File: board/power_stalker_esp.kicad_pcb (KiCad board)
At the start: 2 copper layers, 43.5 x 61 mm, 10 parts, among them J1 POWER IN, J2 LEFT, J3 RIGHT, Q1 Phototrans, Q2 Q_NPN_BEC, U1 74HC393

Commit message: Generated gerber files.
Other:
- board text added: "REV A 11/2018"
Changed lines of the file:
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@@
   (general
     (thickness 1.6)
-    (drawings 746)
+    (drawings 747)
     (tracks 104)
     (zones 0)
@@
     (visible_elements 7FFFFFFF)
     (pcbplotparams
-      (layerselection 0x010fc_ffffffff)
+      (layerselection 0x010f0_ffffffff)
       (usegerberextensions false)
       (usegerberattributes false)
@@
       (outputformat 1)
       (mirror false)
-      (drillshape 1)
+      (drillshape 0)
       (scaleselection 1)
-      (outputdirectory ""))
+      (outputdirectory "Gerbers"))
   )
   (net 0 "")
@@
     )
   )
+  (gr_text "REV A\n11/2018" (at 97.6 115.8) (layer B.SilkS)
+    (effects (font (size 1.5 1.5) (thickness 0.3)) (justify mirror))
+  )
   (gr_line (start 94.725 126.9) (end 94.025 126.9) (layer F.SilkS) (width 0.2))

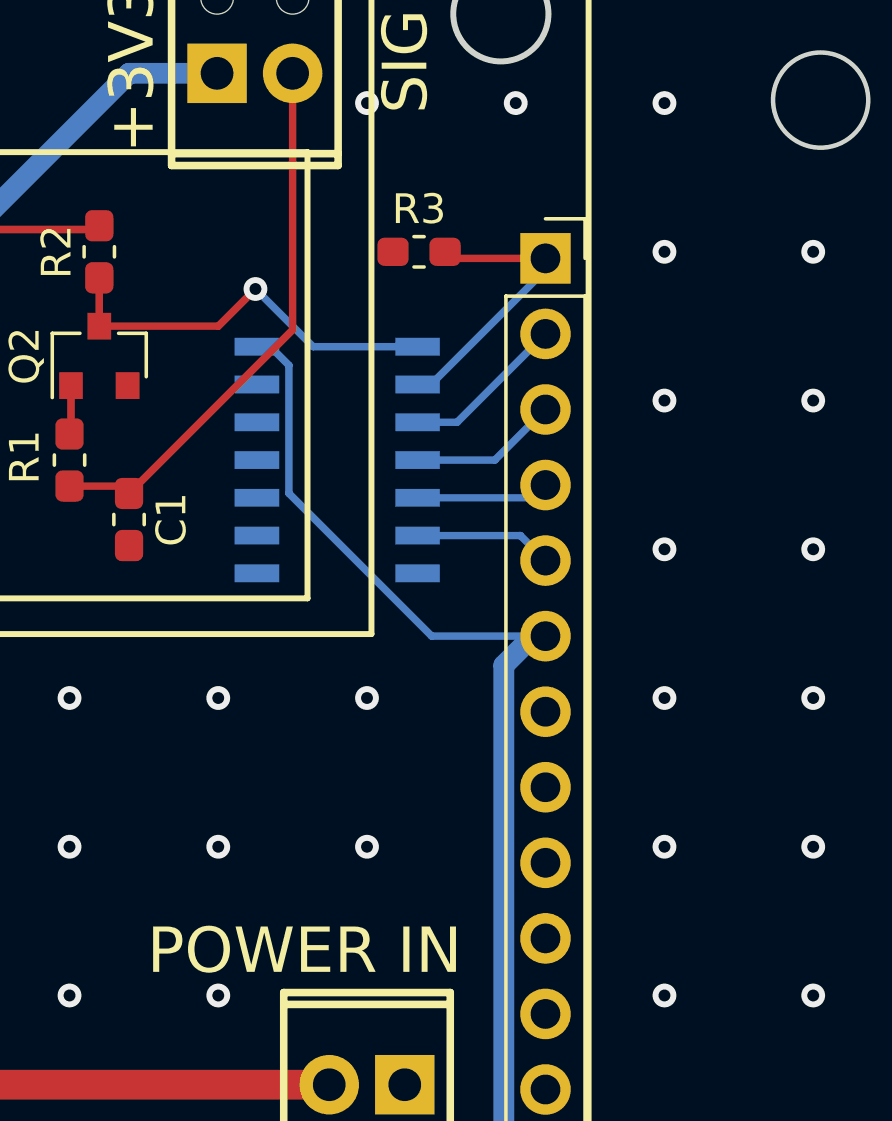
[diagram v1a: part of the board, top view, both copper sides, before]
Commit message: /!\ Moved some GPIO (D0,D3 and D4 seem to not be real GPIOs...)
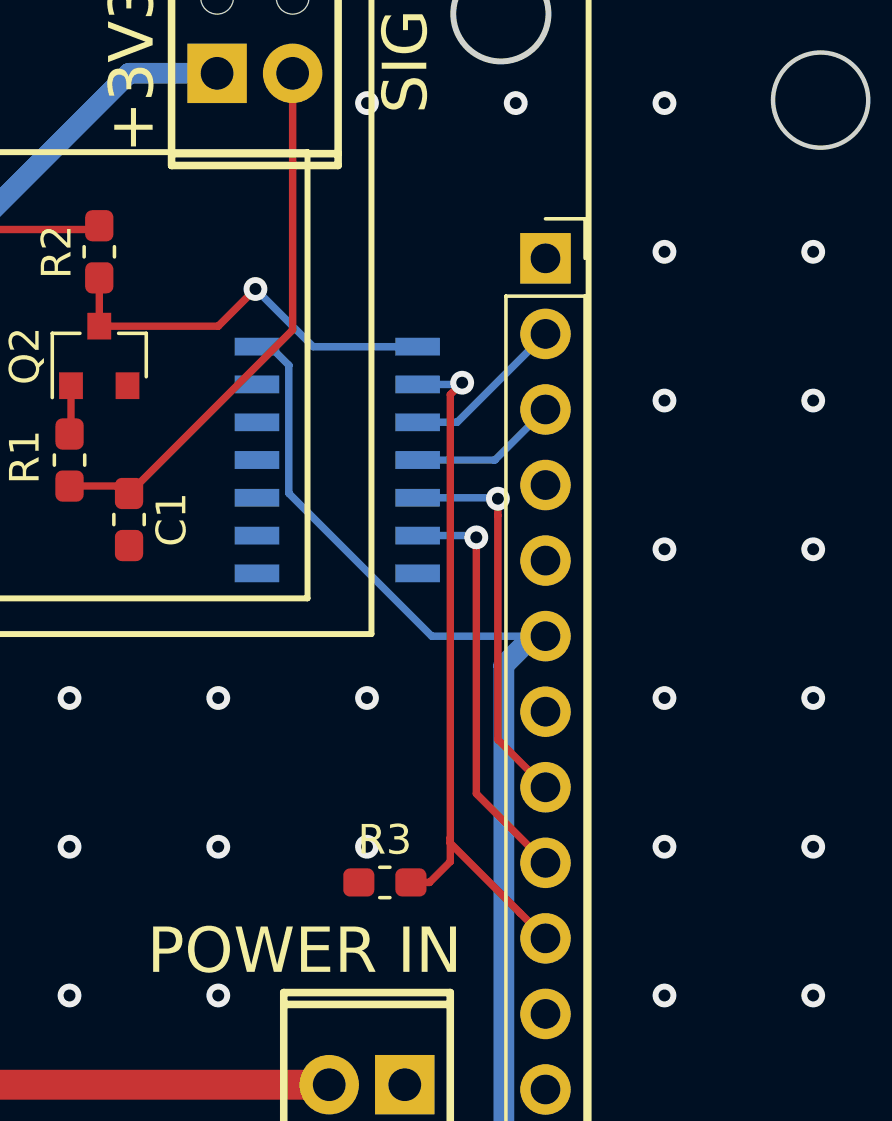
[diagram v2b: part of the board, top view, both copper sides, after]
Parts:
- C1: value 0.1uF/25V -> 0.1uF/50V
- moved R3 21.2 mm to (100.6, 101.2)
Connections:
- J3 pad 1: MASTER_RESET -> (no net)
- J3 pad 10: (no net) -> MASTER_RESET
- J3 pad 4: 1Q2 -> (no net)
- J3 pad 5: 1Q3 -> (no net)
- J3 pad 8: (no net) -> 1Q2
- J3 pad 9: (no net) -> 1Q3
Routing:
- net MASTER_RESET: track 9.75 -> 24.1 mm, vias 0 -> 1
- net 1Q3: track 4.65 -> 13.9 mm, vias 0 -> 1
- net 1Q2: track 4.48 -> 13.1 mm, vias 0 -> 1
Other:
- board text added: "REV B 06/2019"
- board text removed: "REV A 11/2018"
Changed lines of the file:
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@@
-(kicad_pcb (version 20171130) (host pcbnew "(5.0.1)-3")
+(kicad_pcb (version 20171130) (host pcbnew "(5.1.2)-2")
   (general
     (thickness 1.6)
     (drawings 747)
-    (tracks 104)
+    (tracks 117)
     (zones 0)
     (modules 10)
@@
     (zone_45_only no)
     (trace_min 0.2)
-    (segment_width 0.2)
-    (edge_width 0.2)
     (via_size 0.8)
     (via_drill 0.4)
@@
     (uvia_min_size 0.2)
     (uvia_min_drill 0.1)
+    (edge_width 0.2)
+    (segment_width 0.2)
     (pcb_text_width 0.3)
     (pcb_text_size 1.5 1.5)
@@
     (solder_mask_min_width 0.25)
     (aux_axis_origin 0 0)
-    (grid_origin 79.5 124)
     (visible_elements 7FFFFFFF)
     (pcbplotparams
@@
       (effects (font (size 1 1) (thickness 0.15)))
     )
-    (fp_text value 0.1uF/25V (at 0 1.43 270) (layer F.Fab)
+    (fp_text value 0.1uF/50V (at 0 1.43 270) (layer F.Fab)
       (effects (font (size 1 1) (thickness 0.15)))
     )
@@
     (pad 12 thru_hole oval (at 0 27.94) (size 1.7 1.7) (drill 1) (layers *.Cu *.Mask))
     (pad 11 thru_hole oval (at 0 25.4) (size 1.7 1.7) (drill 1) (layers *.Cu *.Mask))
-    (pad 10 thru_hole oval (at 0 22.86) (size 1.7 1.7) (drill 1) (layers *.Cu *.Mask))
-    (pad 9 thru_hole oval (at 0 20.32) (size 1.7 1.7) (drill 1) (layers *.Cu *.Mask))
-    (pad 8 thru_hole oval (at 0 17.78) (size 1.7 1.7) (drill 1) (layers *.Cu *.Mask))
+    (pad 10 thru_hole oval (at 0 22.86) (size 1.7 1.7) (drill 1) (layers *.Cu *.Mask)
+      (net 9 MASTER_RESET))
+    (pad 9 thru_hole oval (at 0 20.32) (size 1.7 1.7) (drill 1) (layers *.Cu *.Mask)
+      (net 5 1Q3))
+    (pad 8 thru_hole oval (at 0 17.78) (size 1.7 1.7) (drill 1) (layers *.Cu *.Mask)
+      (net 6 1Q2))
     (pad 7 thru_hole oval (at 0 15.24) (size 1.7 1.7) (drill 1) (layers *.Cu *.Mask)
       (net 2 GND))
     (pad 6 thru_hole oval (at 0 12.7) (size 1.7 1.7) (drill 1) (layers *.Cu *.Mask)
       (net 4 +3V3))
-    (pad 5 thru_hole oval (at 0 10.16) (size 1.7 1.7) (drill 1) (layers *.Cu *.Mask)
-      (net 5 1Q3))
-    (pad 4 thru_hole oval (at 0 7.62) (size 1.7 1.7) (drill 1) (layers *.Cu *.Mask)
-      (net 6 1Q2))
+    (pad 5 thru_hole oval (at 0 10.16) (size 1.7 1.7) (drill 1) (layers *.Cu *.Mask))
+    (pad 4 thru_hole oval (at 0 7.62) (size 1.7 1.7) (drill 1) (layers *.Cu *.Mask))
     (pad 3 thru_hole oval (at 0 5.08) (size 1.7 1.7) (drill 1) (layers *.Cu *.Mask)
       (net 7 1Q1))
     (pad 2 thru_hole oval (at 0 2.54) (size 1.7 1.7) (drill 1) (layers *.Cu *.Mask)
       (net 8 1Q0))
-    (pad 1 thru_hole rect (at 0 0) (size 1.7 1.7) (drill 1) (layers *.Cu *.Mask)
-      (net 9 MASTER_RESET))
+    (pad 1 thru_hole rect (at 0 0) (size 1.7 1.7) (drill 1) (layers *.Cu *.Mask))
     (model ${KISYS3DMOD}/Connector_PinSocket_2.54mm.3dshapes/PinSocket_1x15_P2.54mm_Vertical.wrl
       (at (xyz 0 0 0))
@@
   )
   (module Resistor_SMD:R_0603_1608Metric_Pad1.05x0.95mm_HandSolder (layer F.Cu)
-    (at 101.75 80)
+    (at 100.6 101.2)
     (descr "Resistor SMD 0603 (1608 Metric), square (rectangular) end terminal, IPC_7351 nominal with elongated pad for handsoldering. (Body size source: http://www.tortai-tech.com/upload/download/2011102023233369053.pdf), generated with kicad-footprint-generator")
     (tags "resistor handsolder")
@@
     )
   )
-  (gr_text "REV A\n11/2018" (at 97.6 115.8) (layer B.SilkS)
+  (gr_text "REV B\n06/2019" (at 97.6 115.8) (layer B.SilkS)
     (effects (font (size 1.5 1.5) (thickness 0.3)) (justify mirror))
   )
@@
   (segment (start 90.875 79.25) (end 91 79.125) (width 0.25) (layer F.Cu) (net 4))
   (segment (start 86.75 79.25) (end 90.875 79.25) (width 0.25) (layer F.Cu) (net 4))
-  (segment (start 105.16 89.54) (end 106 90.38) (width 0.25) (layer B.Cu) (net 5))
-  (segment (start 101.7 89.54) (end 105.16 89.54) (width 0.25) (layer B.Cu) (net 5))
-  (segment (start 105.57 88.27) (end 106 87.84) (width 0.25) (layer B.Cu) (net 6))
-  (segment (start 101.7 88.27) (end 105.57 88.27) (width 0.25) (layer B.Cu) (net 6))
+  (via (at 103.675002 89.6) (size 0.8) (drill 0.4) (layers F.Cu B.Cu) (net 5))
+  (segment (start 101.7 89.54) (end 103.615002 89.54) (width 0.25) (layer B.Cu) (net 5))
+  (segment (start 103.615002 89.54) (end 103.675002 89.6) (width 0.25) (layer B.Cu) (net 5))
+  (segment (start 103.675002 98.215002) (end 106 100.54) (width 0.25) (layer F.Cu) (net 5))
+  (segment (start 103.675002 89.6) (end 103.675002 98.215002) (width 0.25) (layer F.Cu) (net 5))
+  (via (at 104.400002 88.3) (size 0.8) (drill 0.4) (layers F.Cu B.Cu) (net 6))
+  (segment (start 101.7 88.27) (end 104.370002 88.27) (width 0.25) (layer B.Cu) (net 6))
+  (segment (start 104.370002 88.27) (end 104.400002 88.3) (width 0.25) (layer B.Cu) (net 6))
+  (segment (start 106 98) (end 104.400002 96.400002) (width 0.25) (layer F.Cu) (net 6))
+  (segment (start 104.400002 96.400002) (end 104.400002 88.865685) (width 0.25) (layer F.Cu) (net 6))
+  (segment (start 104.400002 88.865685) (end 104.400002 88.3) (width 0.25) (layer F.Cu) (net 6))
   (segment (start 104.3 87) (end 106 85.3) (width 0.25) (layer B.Cu) (net 7))
   (segment (start 101.7 87) (end 104.3 87) (width 0.25) (layer B.Cu) (net 7))
   (segment (start 103.03 85.73) (end 106 82.76) (width 0.25) (layer B.Cu) (net 8))
   (segment (start 101.7 85.73) (end 103.03 85.73) (width 0.25) (layer B.Cu) (net 8))
-  (segment (start 106 80.61) (end 106 80.22) (width 0.25) (layer B.Cu) (net 9))
-  (segment (start 102.15 84.46) (end 106 80.61) (width 0.25) (layer B.Cu) (net 9))
-  (segment (start 101.7 84.46) (end 102.15 84.46) (width 0.25) (layer B.Cu) (net 9))
-  (segment (start 102.845 80.22) (end 102.625 80) (width 0.25) (layer F.Cu) (net 9))
-  (segment (start 106 80.22) (end 102.845 80.22) (width 0.25) (layer F.Cu) (net 9))
+  (via (at 103.2 84.4) (size 0.8) (drill 0.4) (layers F.Cu B.Cu) (net 9))
+  (segment (start 101.7 84.46) (end 103.14 84.46) (width 0.25) (layer B.Cu) (net 9))
+  (segment (start 103.14 84.46) (end 103.2 84.4) (width 0.25) (layer B.Cu) (net 9))
+  (segment (start 105.150001 102.230001) (end 106 103.08) (width 0.25) (layer F.Cu) (net 9))
+  (segment (start 102.800001 99.880001) (end 105.150001 102.230001) (width 0.25) (layer F.Cu) (net 9))
+  (segment (start 103.2 84.4) (end 102.800001 84.799999) (width 0.25) (layer F.Cu) (net 9))
+  (segment (start 102.800001 100.499999) (end 102.800001 99.700001) (width 0.25) (layer F.Cu) (net 9))
+  (segment (start 102.1 101.2) (end 102.800001 100.499999) (width 0.25) (layer F.Cu) (net 9))
+  (segment (start 101.475 101.2) (end 102.1 101.2) (width 0.25) (layer F.Cu) (net 9))
+  (segment (start 102.800001 99.700001) (end 102.800001 99.880001) (width 0.25) (layer F.Cu) (net 9))
+  (segment (start 102.800001 84.799999) (end 102.800001 99.700001) (width 0.25) (layer F.Cu) (net 9))
   (segment (start 90.05 86.075) (end 90 86.125) (width 0.25) (layer F.Cu) (net 10))
   (segment (start 90.05 84.5) (end 90.05 86.075) (width 0.25) (layer F.Cu) (net 10))

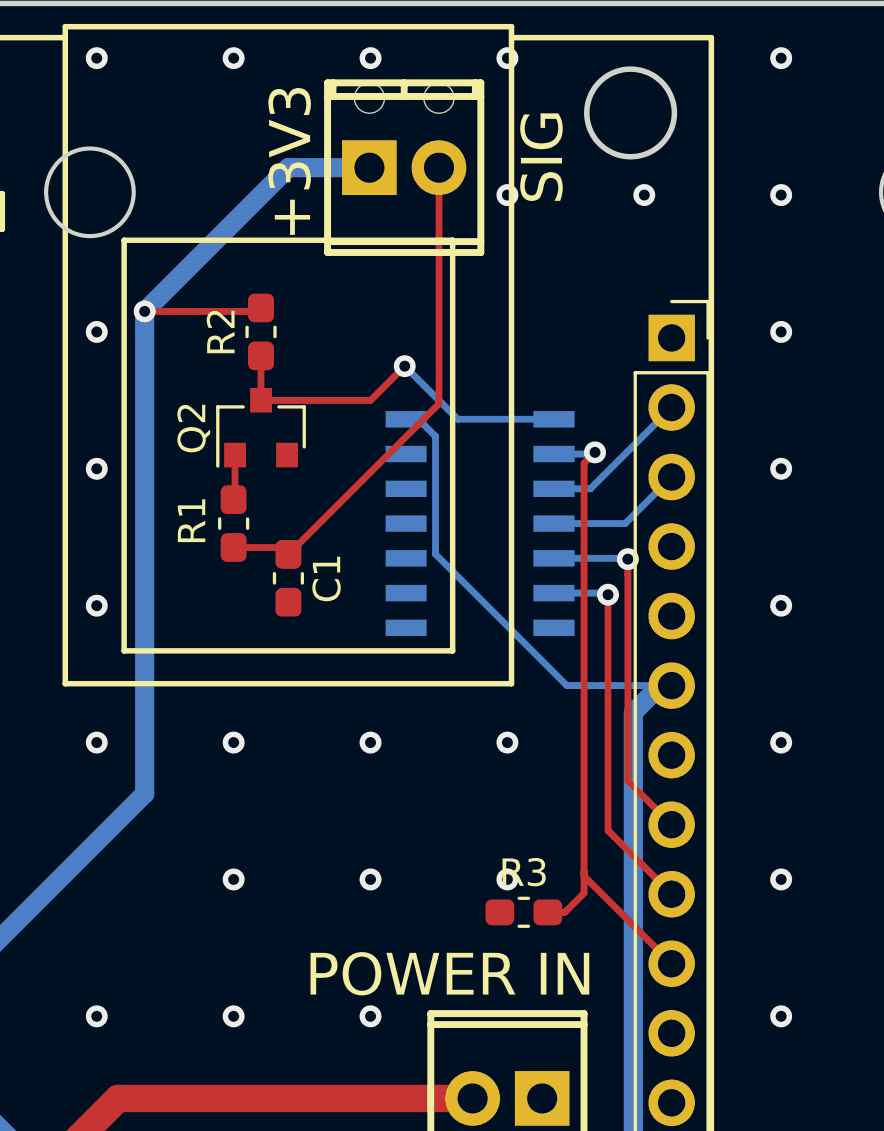
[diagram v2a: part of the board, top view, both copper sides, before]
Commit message: Reworked input circuit.
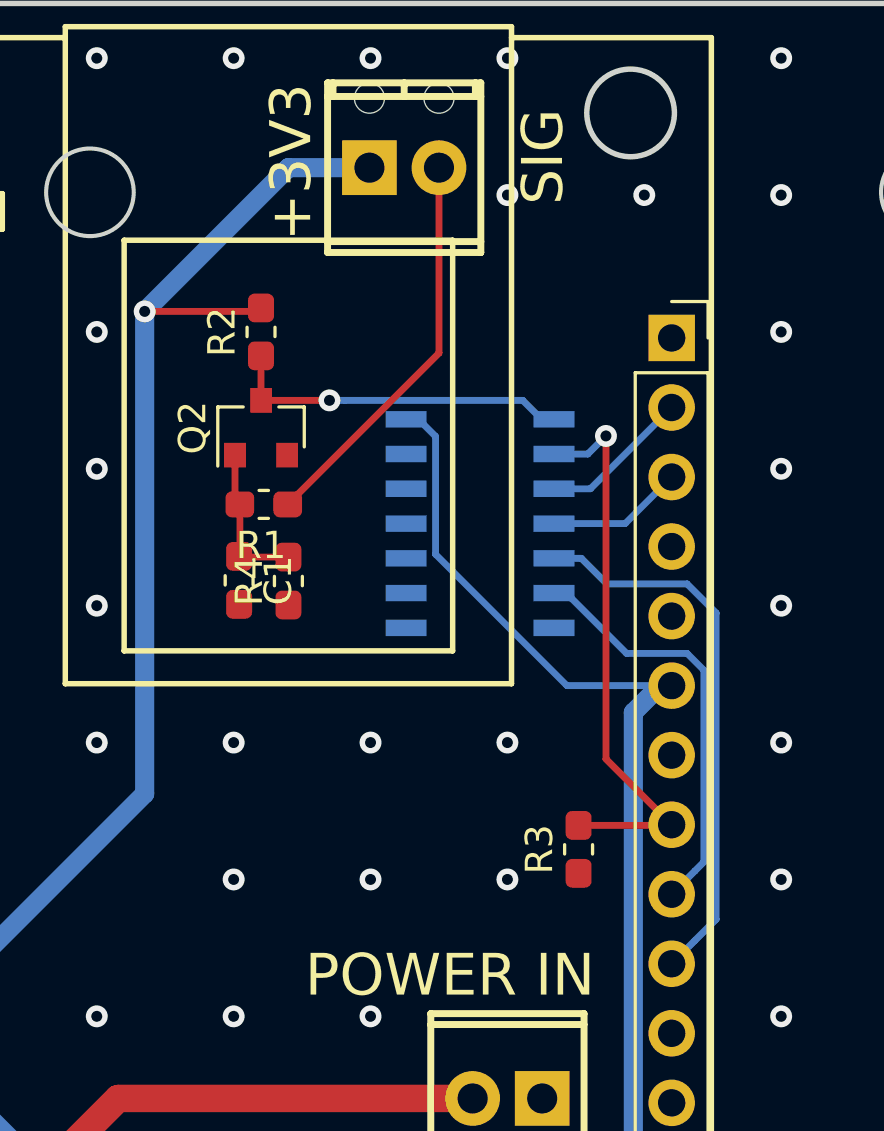
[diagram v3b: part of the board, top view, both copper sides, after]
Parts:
- added R4: 10k, Resistor_SMD:R_0603_1608Metric_Pad1.05x0.95mm_HandSolder, F.Cu at (92.0, 89.1)
- R1: value 100k -> 10k
- moved R3 3.05 mm to (102.6, 98.9), turned to 90 degrees
- moved C1 1.80 mm to (90.2, 89.1)
- moved R1 1.30 mm to (91.1, 86.3), turned to 0 degrees
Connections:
- J3 pad 10: MASTER_RESET -> 1Q2
- J3 pad 8: 1Q2 -> MASTER_RESET
- Q1 pad 2: Net-(C1-Pad1) -> Net-(Q1-Pad2)
- Q2 pad 1: Net-(Q2-Pad1) -> Net-(C1-Pad1)
- R1 pad 1: Net-(Q2-Pad1) -> Net-(C1-Pad1)
- R1 pad 2: Net-(C1-Pad1) -> Net-(Q1-Pad2)
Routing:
- net Net-(Q1-Pad2): track 0.00 -> 14.6 mm
- net Net-(C1-Pad1): track 18.5 -> 5.59 mm
- net 1Q2: track 13.1 -> 20.2 mm, vias 1 -> 0
- net MASTER_RESET: track 24.1 -> 20.8 mm
- net Net-(Q2-Pad1): track 1.65 -> 0.00 mm
- net 1Q3: track 13.9 -> 15.3 mm, vias 1 -> 0
- net Net-(Q2-Pad3): track 13.6 -> 12.6 mm
